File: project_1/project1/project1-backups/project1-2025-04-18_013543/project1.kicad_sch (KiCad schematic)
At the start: 45 parts, among them Q1 2N3904, Q2 2N3906, T1 120AC12AC, U1 TL071, U2 LM317, U3 LM337, U4 OPA124U, U5 L7805, U6 TL084, U7 TL071, U8 TL071

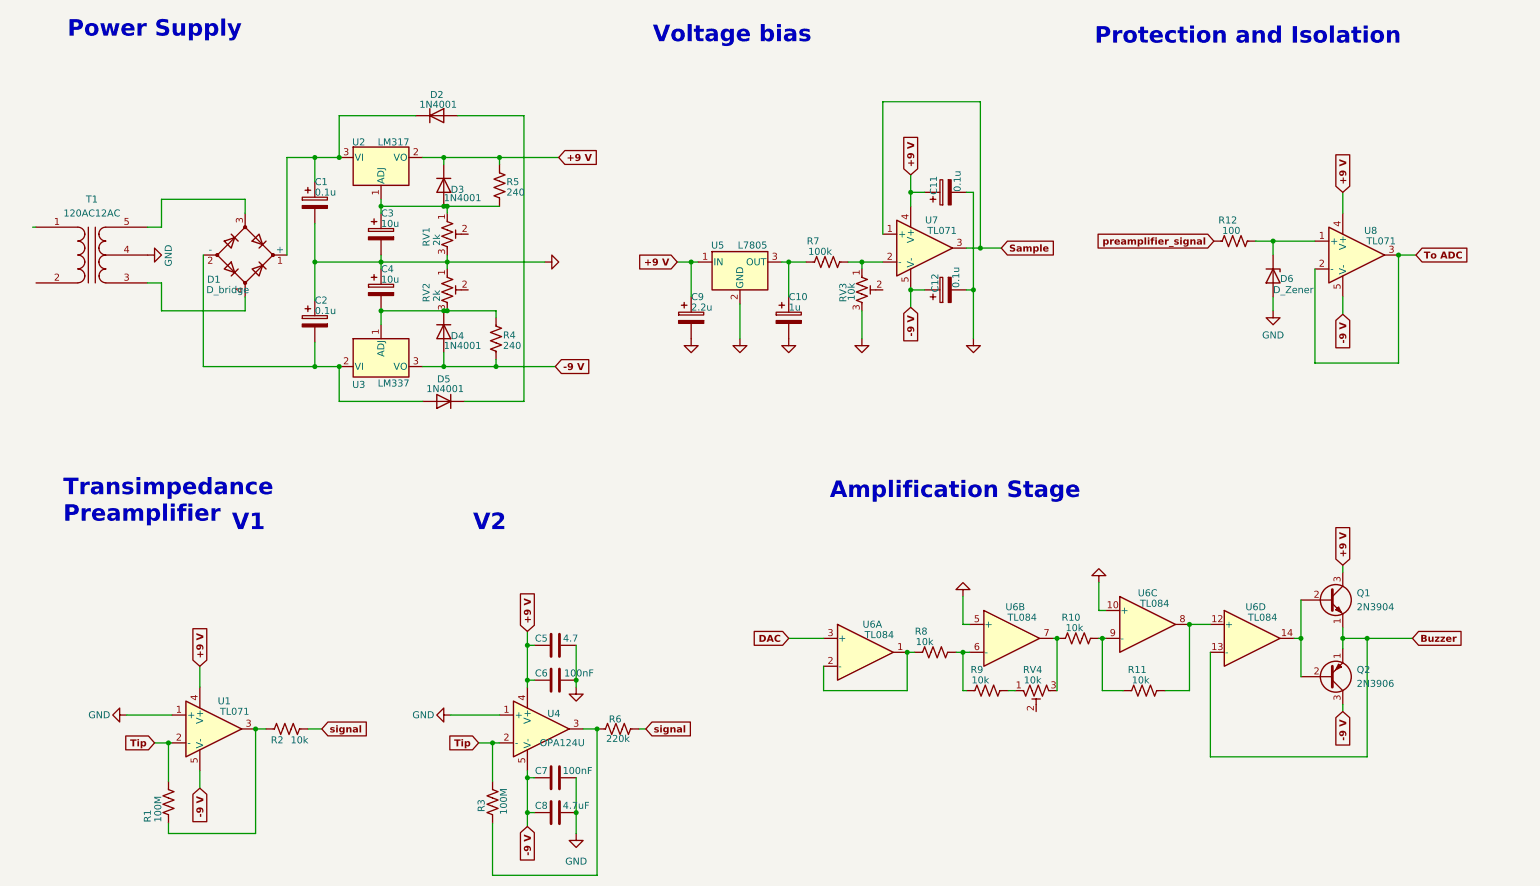
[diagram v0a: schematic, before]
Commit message: agregando los repositorios del STM version pro ademas de la fuente de pm17VDC +5V para el ESP32.
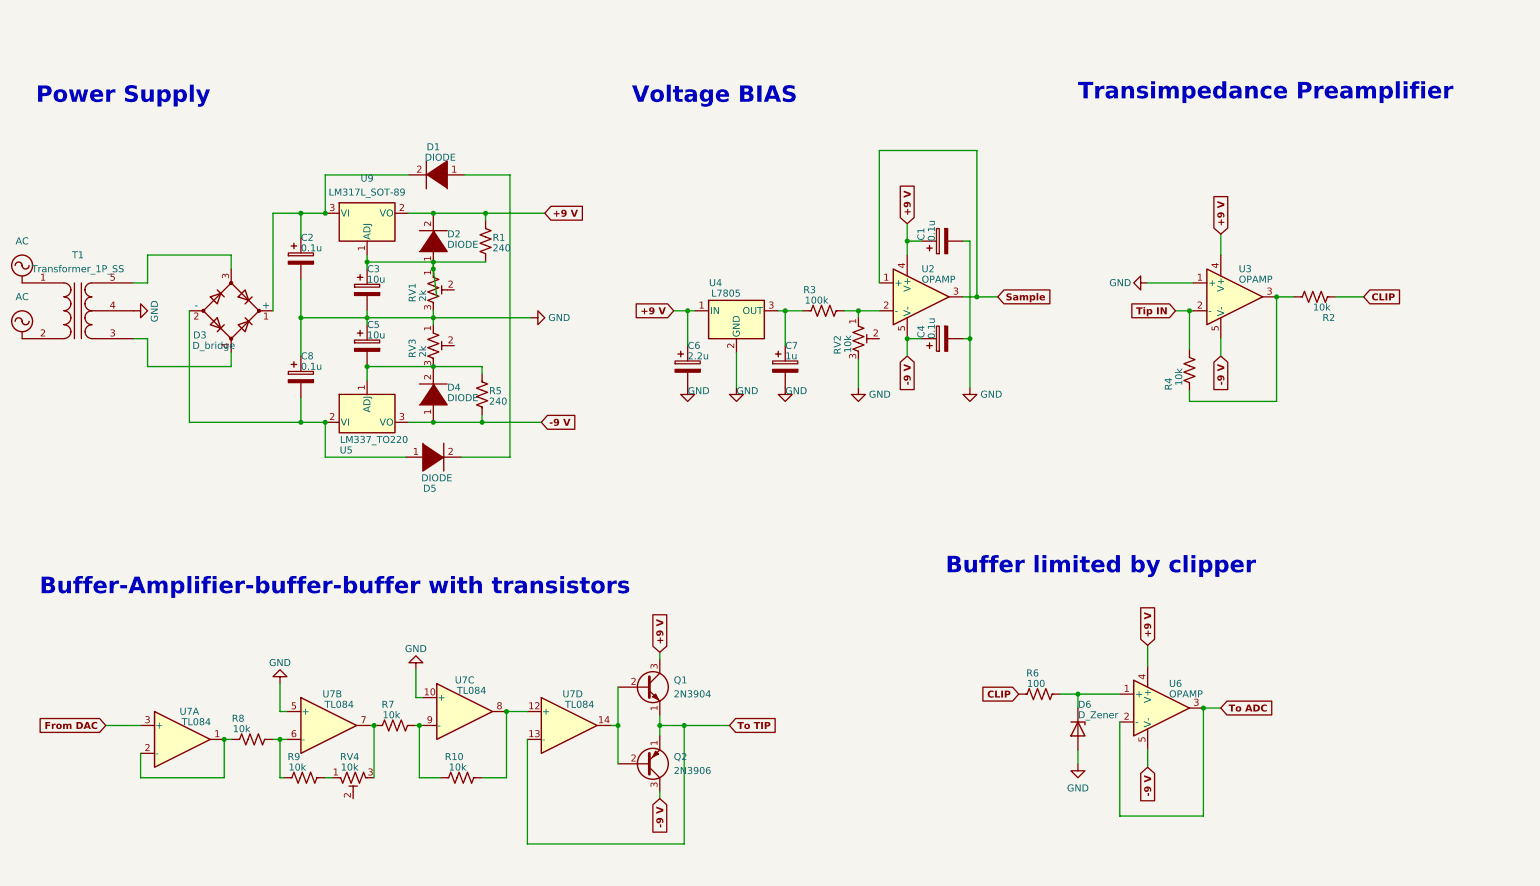
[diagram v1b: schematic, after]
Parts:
- removed C5: 4.7, symbol Device:C
- removed C6, C7: 100nF, symbol Device:C
- removed C8: 4.7uF, symbol Device:C
- removed D2, D3, D4, D5: 1N4001, Diode_THT:D_DO-41_SOD81_P10.16mm_Horizontal, symbol Diode:1N4001
- removed R3: 100M, symbol Device:R_US
- removed R6: 220k, symbol Device:R_US
- removed U4: OPA124U, symbol pspice:OPAMP
- added D1, D2, D4, D5: DIODE, symbol pspice:DIODE
- R4: renamed from R1; value 100M -> 10k
- T1: value 120AC12AC -> Transformer_1P_SS
- U2: renamed from U7; value TL071 -> OPAMP
- U3: renamed from U1; value TL071 -> OPAMP
- U5: renamed from U3; value LM337 -> LM337_TO220
- U6: renamed from U8; value TL071 -> OPAMP
- U9: renamed from U2; value LM317 -> LM317L_SOT-89
- renumbered C11 to C1, C1 to C2, C12 to C4, C4 to C5, C9 to C6, C10 to C7, C2 to C8, D1 to D3, R5 to R1, R11 to R10, R7 to R3, R4 to R5, R12 to R6, R10 to R7, RV3 to RV2, RV2 to RV3, U5 to U4, U6 to U7
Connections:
- net signal is gone; now on net CLIP: R2.2
- net +9 V: now also D2.2 (A)
- net -9 V: now also D4.1 (K)
- net at C8.2, D3.2 (-), U5.2 (VI): now also D5.1 (K)
- net at C3.1, R1.1, RV1.1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: now also D2.1 (K)
- net AC: now reaches T1.1 (AA)
- net AC: now also T1.2 (AB)
- net at C5.2, R5.2, RV3.3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: now also D4.2 (A)
- net at C2.1, D3.1 (+), U9.3 (VI): now also D1.2 (A)
- net Buzzer renamed To TIP
- net DAC renamed From DAC
- net Tip renamed Tip IN
- net preamplifier_signal renamed CLIP
- new net: D1.1 (K), D5.2 (A)
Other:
- note added: "Buffer limited by clipper"
- note added: "Buffer-Amplifier-buffer-buffer with transistors"
- note added: "Voltage BIAS"
- note removed: "Amplification Stage"
- note removed: "Protection and Isolation"
- note removed: "V1"
- note removed: "V2"
- note removed: "Voltage bias"
- moved on the sheet: C1, C2, C3, C4, C5, C6, C7, C8, D3, D6, Q1, Q2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
